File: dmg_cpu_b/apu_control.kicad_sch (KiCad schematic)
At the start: 79 parts

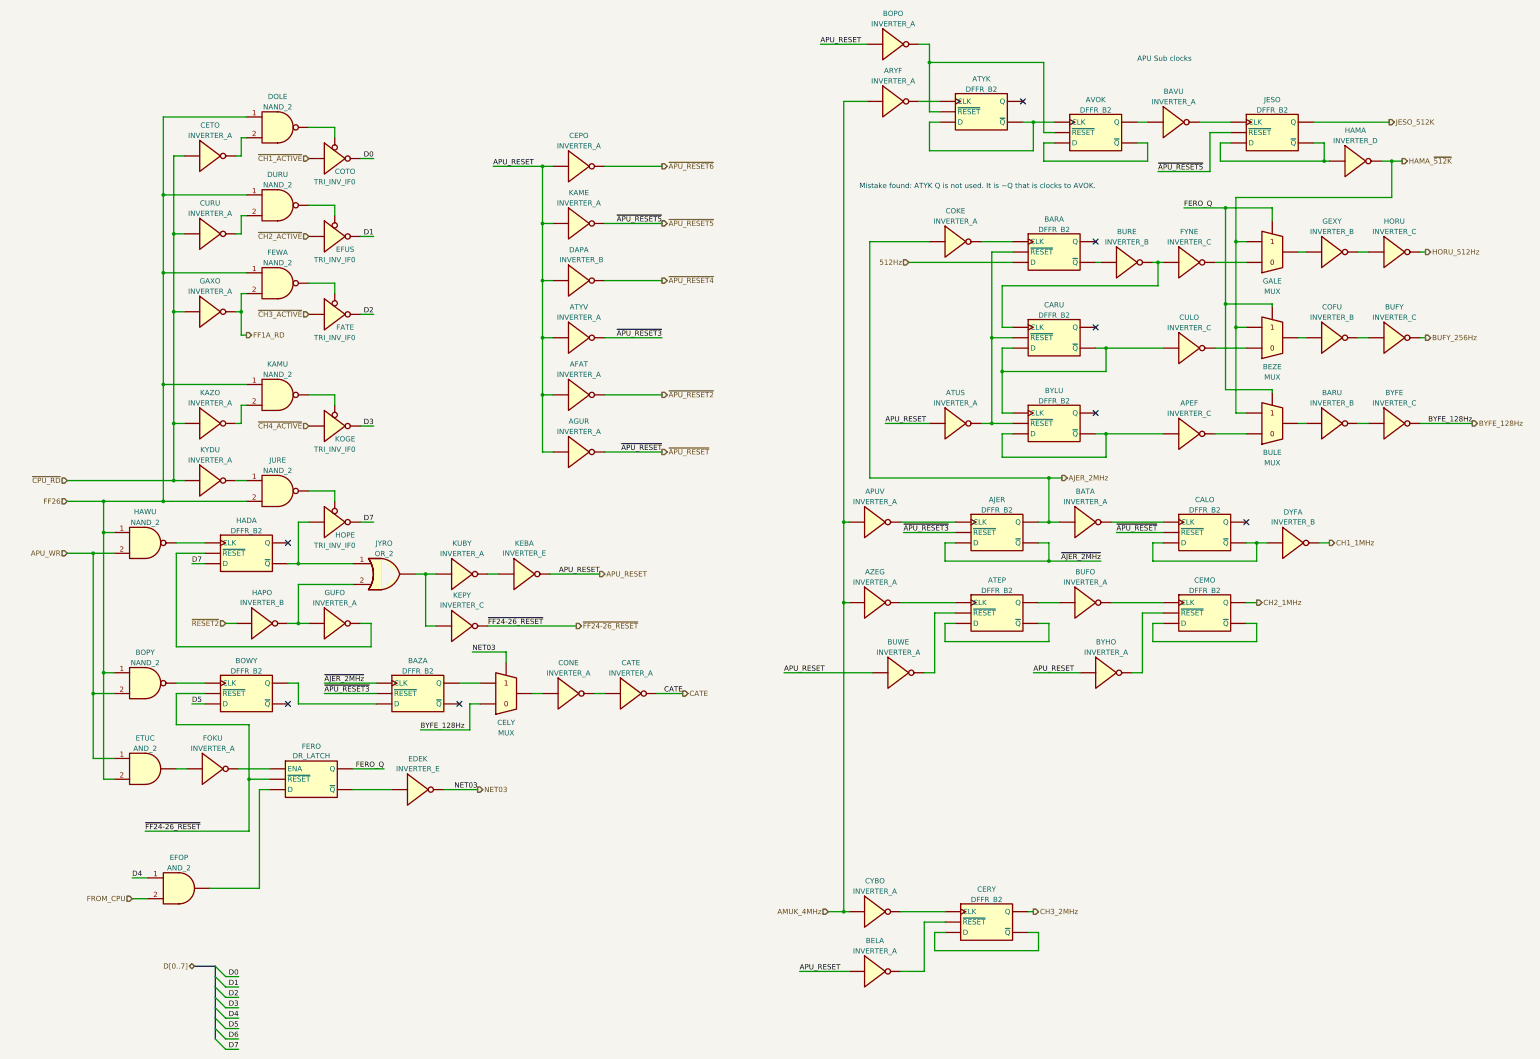
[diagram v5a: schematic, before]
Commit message: Fixes made from issues, channel 4 sheet aded and tidy up of hierarchical APU sheet. Small fixes done here and there when doing ERC.
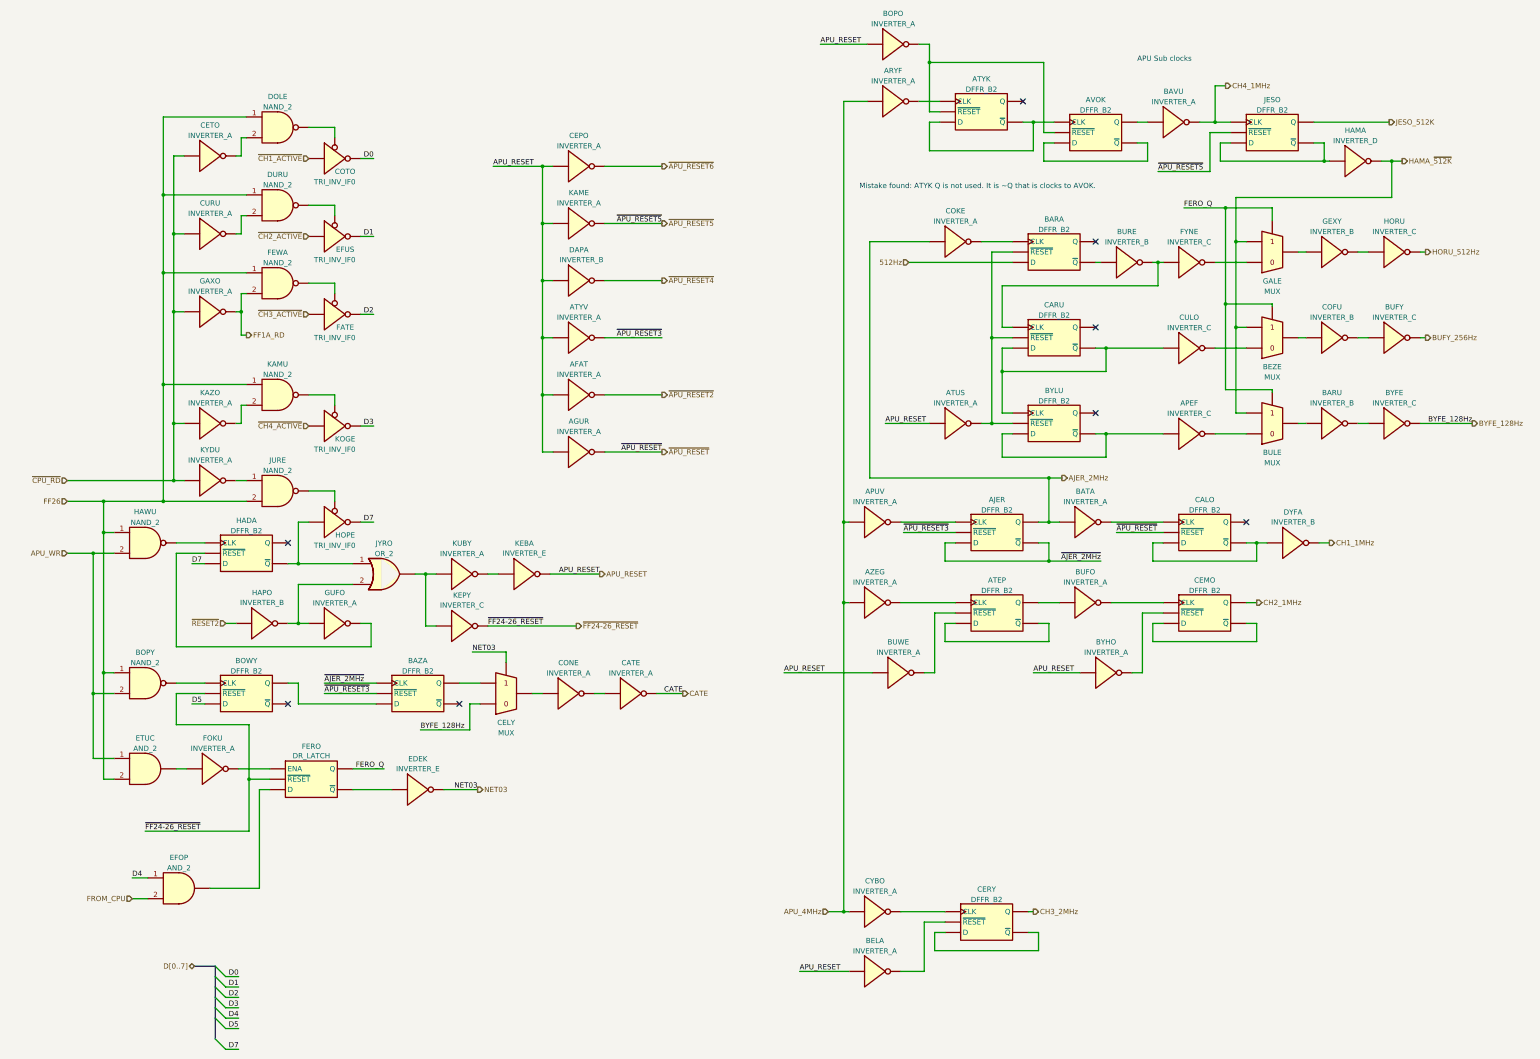
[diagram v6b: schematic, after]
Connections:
- net CH4_1MHz: now reaches BAVU.2, JESO.1 (CLK)
- net AMUK_4MHz renamed APU_4MHz
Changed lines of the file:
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@@
   (junction (at 370.84 53.975) (diameter 0) (color 0 0 0 0)
+  )
+  (junction (at 327.66 44.45) (diameter 0) (color 0 0 0 0)
   )
   (junction (at 53.34 184.15) (diameter 0) (color 0 0 0 0)
@@
     (stroke (width 0) (type default) (color 0 0 0 0))
   )
-  (bus_entry (at 83.185 266.065) (size 2.54 2.54)
-    (stroke (width 0) (type default) (color 0 0 0 0))
-  )
   (bus_entry (at 83.185 260.985) (size 2.54 2.54)
     (stroke (width 0) (type default) (color 0 0 0 0))
@@
     (stroke (width 0) (type default) (color 0 0 0 0))
   )
-  (bus (pts (xy 83.185 266.065) (xy 83.185 263.525))
+  (bus (pts (xy 83.185 263.525) (xy 83.185 268.605))
     (stroke (width 0) (type default) (color 0 0 0 0))
   )
@@
     (stroke (width 0) (type default) (color 0 0 0 0))
   )
-  (wire (pts (xy 323.85 44.45) (xy 331.47 44.45))
+  (wire (pts (xy 323.85 44.45) (xy 327.66 44.45))
     (stroke (width 0) (type default) (color 0 0 0 0))
   )
@@
     (stroke (width 0) (type default) (color 0 0 0 0))
   )
+  (wire (pts (xy 327.66 44.45) (xy 331.47 44.45))
+    (stroke (width 0) (type default) (color 0 0 0 0))
+  )
   (wire (pts (xy 53.34 200.025) (xy 58.42 200.025))
     (stroke (width 0) (type default) (color 0 0 0 0))
@@
     (stroke (width 0) (type default) (color 0 0 0 0))
   )
+  (wire (pts (xy 327.66 35.56) (xy 330.2 35.56))
+    (stroke (width 0) (type default) (color 0 0 0 0))
+  )
   (wire (pts (xy 192.405 97.155) (xy 178.435 97.155))
     (stroke (width 0) (type default) (color 0 0 0 0))
@@
     (stroke (width 0) (type default) (color 0 0 0 0))
   )
+  (wire (pts (xy 327.66 35.56) (xy 327.66 44.45))
+    (stroke (width 0) (type default) (color 0 0 0 0))
+  )
   (wire (pts (xy 73.66 191.77) (xy 91.44 191.77))
     (stroke (width 0) (type default) (color 0 0 0 0))
@@
     (stroke (width 0) (type default) (color 0 0 0 0))
   )
-  (bus (pts (xy 83.185 268.605) (xy 83.185 266.065))
-    (stroke (width 0) (type default) (color 0 0 0 0))
-  )
   (wire (pts (xy 273.05 97.155) (xy 273.05 118.11))
     (stroke (width 0) (type default) (color 0 0 0 0))
@@
   )
   (wire (pts (xy 285.75 53.975) (xy 285.75 49.53))
-    (stroke (width 0) (type default) (color 0 0 0 0))
-  )
-  (wire (pts (xy 85.725 268.605) (xy 88.9 268.605))
     (stroke (width 0) (type default) (color 0 0 0 0))
   )
@@
     (effects (font (size 1.27 1.27)) (justify left bottom))
   )
-  (label "D6" (at 88.9 268.605 180)
-    (effects (font (size 1.27 1.27)) (justify right bottom))
-  )
   (label "APU_RESET" (at 222.25 179.07 0)
     (effects (font (size 1.27 1.27)) (justify left bottom))
@@
   (label "~{APU_RESET}" (at 192.405 125.095 180)
     (effects (font (size 1.27 1.27)) (justify right bottom))
+  )
+  (hierarchical_label "CH4_1MHz" (shape output) (at 330.2 35.56 0)
+    (effects (font (size 1.27 1.27)) (justify left))
   )
   (hierarchical_label "FF1A_RD" (shape output) (at 90.805 96.52 0)
@@
     (effects (font (size 1.27 1.27)) (justify left))
   )
-  (hierarchical_label "AMUK_4MHz" (shape input) (at 233.045 237.49 180)
+  (hierarchical_label "APU_4MHz" (shape input) (at 233.045 237.49 180)
     (effects (font (size 1.27 1.27)) (justify right))
   )

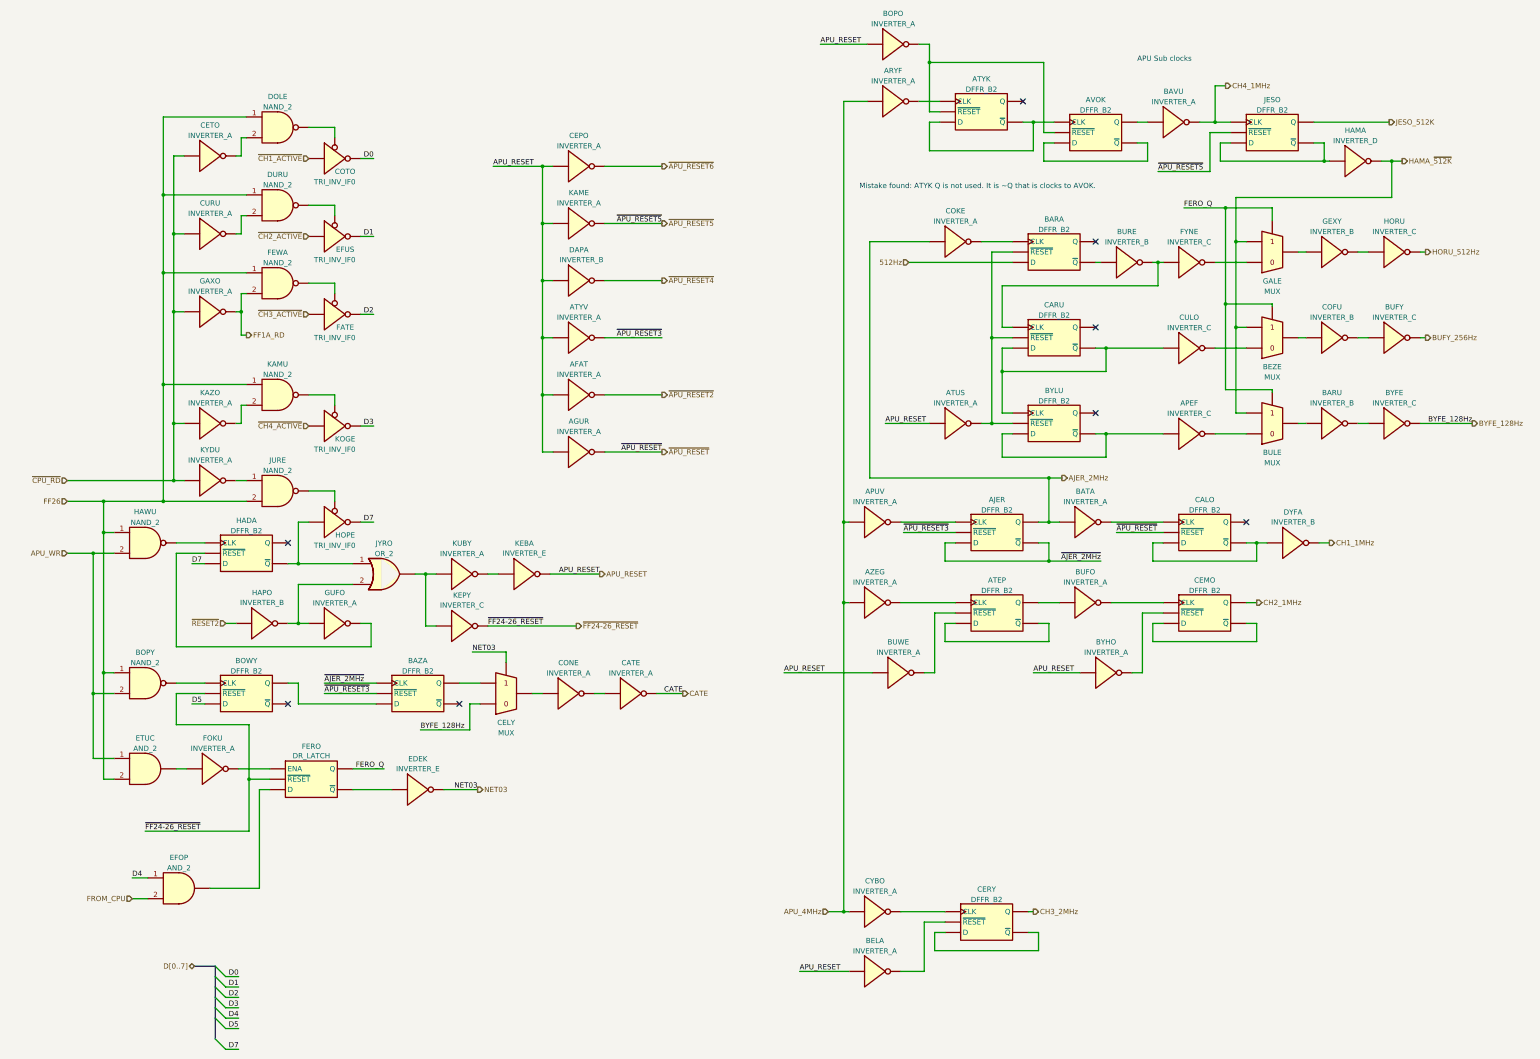
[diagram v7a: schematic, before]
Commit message: Fixes made based on raised issues. PPU decode page added as draft level.
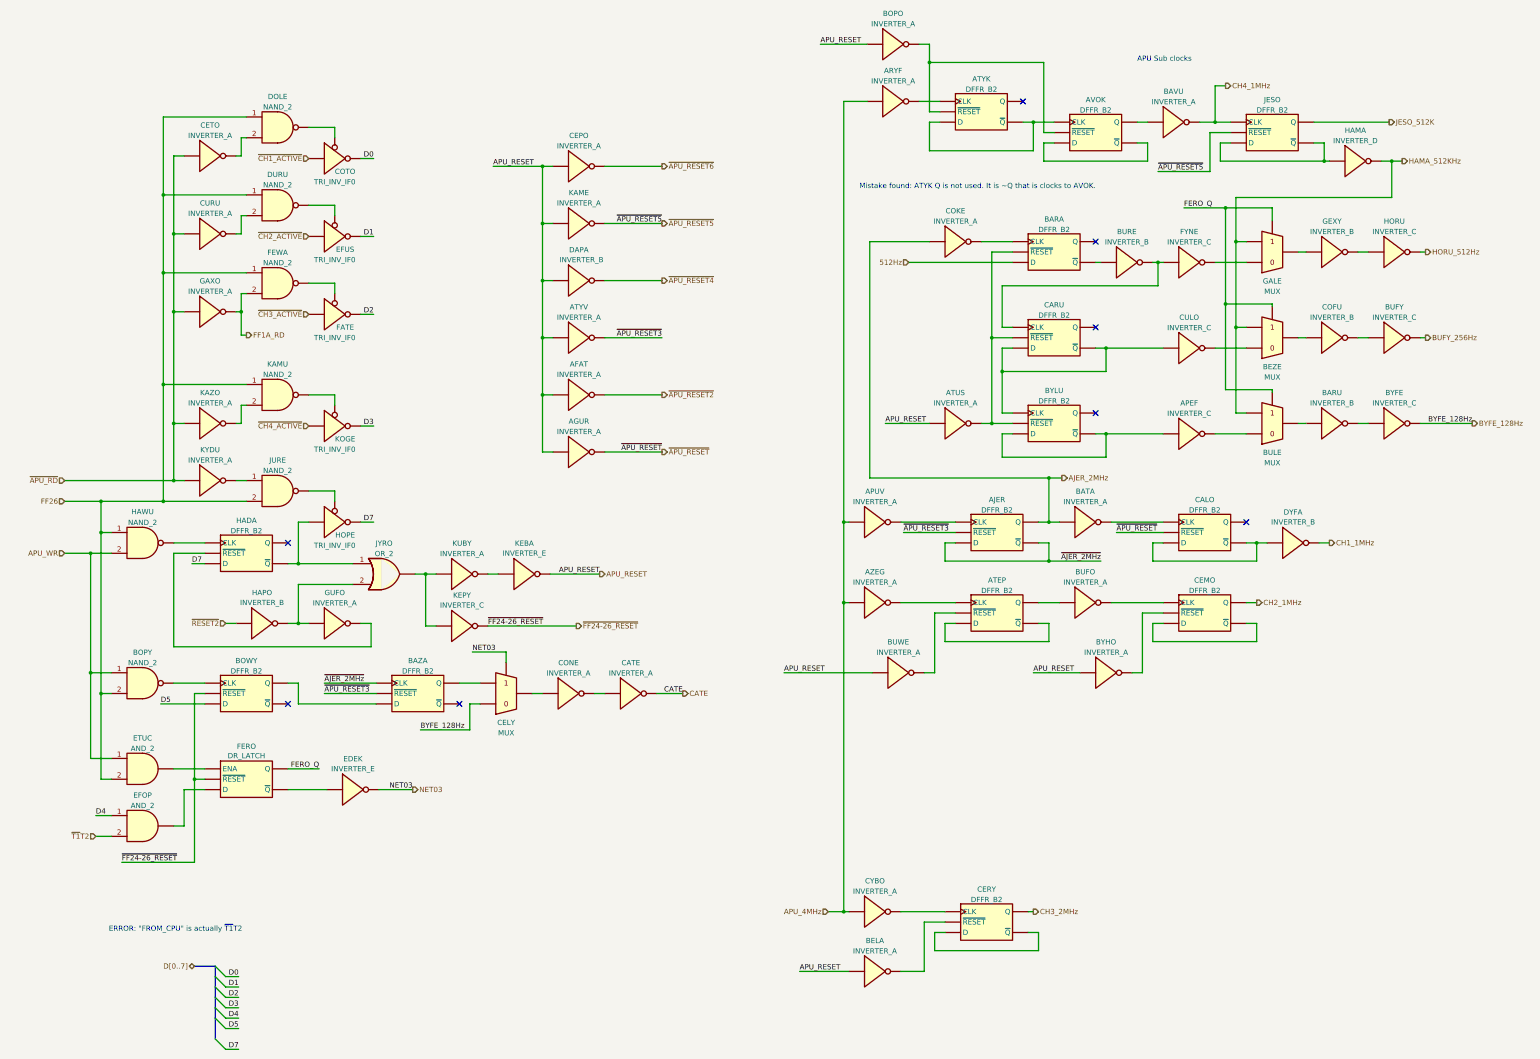
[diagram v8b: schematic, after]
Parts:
- removed FOKU: INVERTER_A, symbol DMG_CPU_Cells:INVERTER_A
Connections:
- net APU_WR: now also BOPY.1; no longer BOPY.2
- net FF26: now also BOPY.2; no longer BOPY.1
- net at ETUC.3: now also FERO.1 (~{ENA}), FERO.3 (ENA)
- net FROM_CPU renamed ~{T1}T2
- net HAMA_~{512K} renamed HAMA_512KHz
- net ~{CPU_RD} renamed ~{APU_RD}
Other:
- note added: "ERROR: "FROM_CPU" is actually ~{T1}T2"
- moved on the sheet: BOPY, EDEK, EFOP, ETUC, FERO, HAWU
